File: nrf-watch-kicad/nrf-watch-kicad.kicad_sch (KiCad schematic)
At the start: 73 parts, among them IC1 TLV840MAPL36DBVRQ1, IC2 XC9265C181MR-G, IC3 TPS61023DRLT, IC4 MAX30101EFD+T, J1 Conn_ARM_JTAG_SWD_10, M1 Vibrator DC Motor, Q1 DMP2045U-7, Q2 S8050, U1 MAX1811ESA+, U2 DMC2400UV-7, U3 LIS2DS12TR, U4 MX25R6435FZNIL0, U5 u-blox ANNA-B402, U6 DRV2603RUNT, U7 XC9265A331MR-G, U8 TXB0104QRUTRQ1, U9 GC9A01

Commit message: Schematic pretty much done, final review left.
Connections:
- net ~{RESET_BAT_SUP}: now reaches IC1.1 (~{RESET}), IC2.3 (CE), TP7.1
- net TPS_VOUT: now reaches IC3.6 (VOUT), R17.2
- net BASE_BLK: now reaches Q2.2 (B), R14.2, R15.1
- net MOTOR_OUT-: now reaches M1.2 (-), U6.6 (OUT-)
- net MOTOR_OUT+: now reaches M1.1 (+), U6.9 (OUT+)
- net SELI: now reaches R2.1, U1.2 (SELI)
- net MR: now reaches IC1.4 (~{MR}), TP6.1
- net D_VOUT: now reaches L2.1, U7.4 (VOUT)
- net RESET_NN: now reaches J1.10 (~{RESET}), U5.12 (RESET_N/P0.18)
- net SWDIO: now reaches J1.2 (SWDIO/TMS), U5.42 (SWDIO)
- net SWDCLK: now reaches J1.4 (SWDCLK/TCK), U5.41 (SWDCLK)
- net COLLECTOR_BLK: now reaches Q2.3 (C), R16.1
- net DISPLAY_HIGH_DC: now reaches U8.10 (B1), U9.7 (D/C)
- net DISPLAY_HIGH_SDA: now reaches U8.7 (B4), U9.10 (SDA)
- net DISPLAY_HIGH_SCL: now reaches U8.8 (B3), U9.9 (SCL)
- net DISPLAY_HIGH_CS: now reaches U8.9 (B2), U9.8 (CS)
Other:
- note added: "1.8<->3.3 level shifter"
- note added: "5V regulator"
- note added: "Accelerometer and step counter"
- note added: "Biometric sensor Heart rate etc."
- note added: "Display"
- note added: "Display backlight"
- note added: "External 8MB Flash"
- note added: "Microcontroller (NRF52833)"
- note added: "Power Management"
- note added: "Power flags"
- note added: "Pull-up resistors"
- note added: "TODO CHECK if mosfet is correct connected"
- note added: "Vibration motor"
- note removed: "I2C pull-ups"
- note removed: "TODO CHECK if OK"
- company: (none) -> Jakob Krantz
- title: (none) -> Smart Watch
- moved on the sheet: BT1, C1, C10, C11, C12, C13, C14, C15, C16, C17, C18, C2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

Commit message: Started with routing.
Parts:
- removed NT1: NetTie_2, symbol Device:NetTie_2
- removed Q2: S8050, symbol Transistor_BJT:S8050
- removed TP4: GND, TestPoint:TestPoint_Pad_D2.0mm, symbol Connector:TestPoint
- added C19: 4.7uF, Capacitor_SMD:C_0603_1608Metric_Pad1.08x0.95mm_HandSolder, symbol Device:C_Small
- added CHG+1, EXT_VIN1: Conn_01x01_Male, TestPoint:TestPoint_Pad_D1.5mm, symbol Connector:Conn_01x01_Male
- added CHG-1, GND1: Conn_01x01_Male, TestPoint:TestPoint_Pad_1.5x1.5mm, symbol Connector:Conn_01x01_Male
- added Q2: SS8050-G, SamacSys_Parts:SOT95P240X115-3N, symbol SamacSys_Parts:SS8050-G
- BT1: footprint (none) -> Connector_Wire:SolderWire-0.1sqmm_1x02_P3.6mm_D0.4mm_OD1mm
- L1, L2, L3: footprint (none) -> Inductor_SMD:L_0603_1608Metric_Pad1.05x0.95mm_HandSolder
- M1: footprint (none) -> user_library:TestPoint_2Pads_Pitch2.54mm_Drill0.8mm
- TP5, TP8: footprint TestPoint:TestPoint_Pad_D2.0mm -> TestPoint:TestPoint_Pad_D1.0mm
- U5: footprint user_library:ANNA-B402 -> user_library:ANNA-B402_altium_import
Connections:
- net LEDA is gone; now on net DISPLAY_3V3: U9.3 (LEDA)
- net +1V8: now also C19.1
- net BASE_BLK: now also Q2.1
- net BAT_MON: now also U5.27 (GPIO_27/P0.31); no longer U5.24 (GPIO_24/P0.05)
- net BAT_MON_EN: now also U5.28 (GPIO_28/P0.30); no longer U5.29 (GPIO_29/P0.29)
- net COLLECTOR_BLK: now also Q2.3
- net DRV_VIB_PWM: now also U5.17 (GPIO_17/P0.00/XL1); no longer U5.33 (GPIO_33/P0.26)
- net GND: now also C19.2, CHG-1.1 (Pin_1), GND1.1 (Pin_1), Q2.2
- net INT1_LIS: now also U5.29 (GPIO_29/P0.29); no longer U5.50 (GPIO_50/P0.08)
- net INT2_LIS: now also U5.30 (GPIO_30/P0.28); no longer U5.11 (GPIO_11/P0.14)
- net VBUS: now also CHG+1.1 (Pin_1)
- net VDDA: now also EXT_VIN1.1 (Pin_1)
- net PWR_B4_BRIDGE: now reaches D1.1, IC1.2 (VDD), JP1.1 (A), Q1.3
- net D2: now reaches R6.1, U2.3 (D2)
- net G2: now reaches R4.2, U2.5 (G2), U2.6 (D1)
- net D_VOUT renamed V_VOUT
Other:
- moved on the sheet: C1

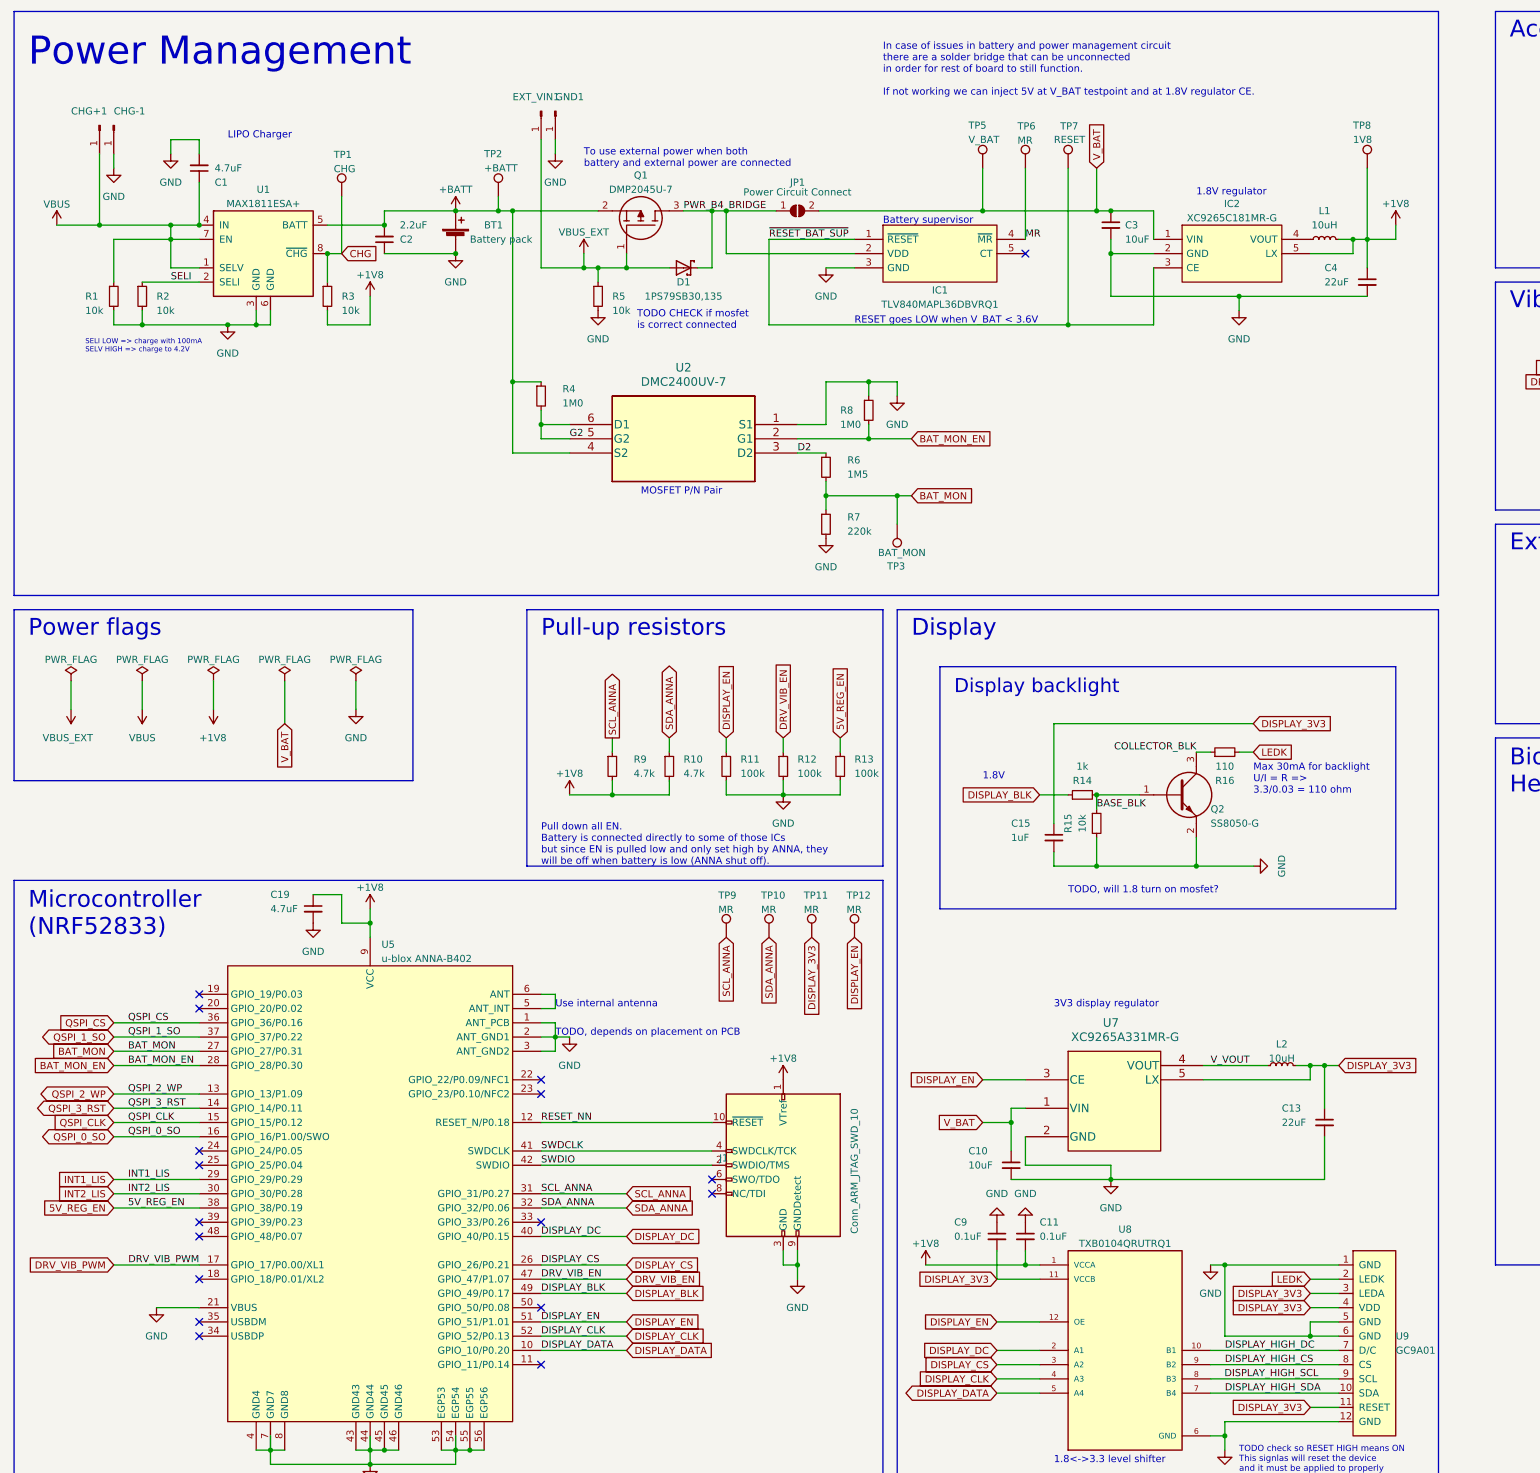
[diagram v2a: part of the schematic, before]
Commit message: Routed power, flash, accelerometer and vibration driver.
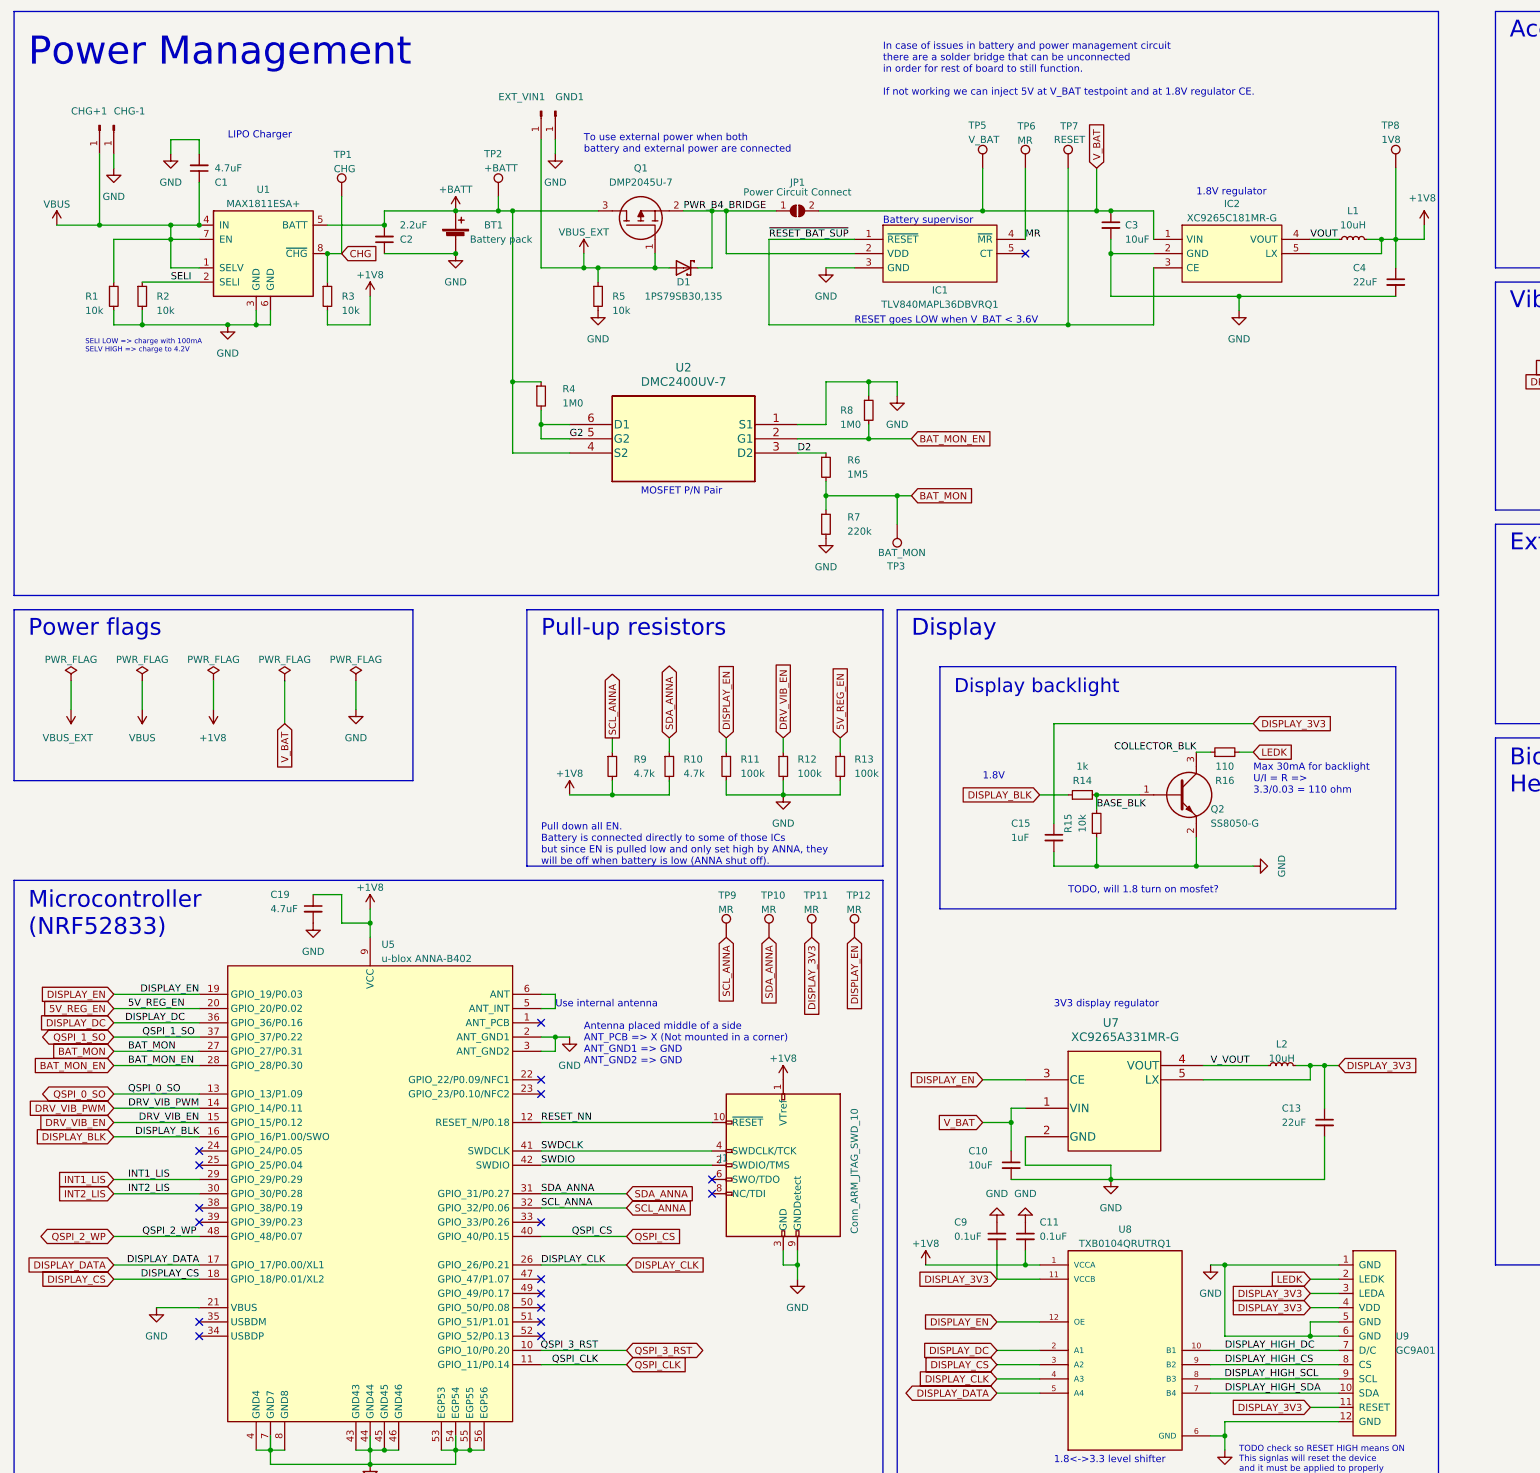
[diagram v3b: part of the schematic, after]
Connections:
- net +BATT: now also Q1.3; no longer Q1.2
- net 5V_REG_EN: now also U5.20 (GPIO_20/P0.02); no longer U5.38 (GPIO_38/P0.19)
- net DISPLAY_BLK: now also U5.16 (GPIO_16/P1.00/SWO); no longer U5.49 (GPIO_49/P0.17)
- net DISPLAY_CLK: now also U5.26 (GPIO_26/P0.21); no longer U5.52 (GPIO_52/P0.13)
- net DISPLAY_CS: now also U5.18 (GPIO_18/P0.01/XL2); no longer U5.26 (GPIO_26/P0.21)
- net DISPLAY_DATA: now also U5.17 (GPIO_17/P0.00/XL1); no longer U5.10 (GPIO_10/P0.20)
- net DISPLAY_DC: now also U5.36 (GPIO_36/P0.16); no longer U5.40 (GPIO_40/P0.15)
- net DISPLAY_EN: now also U5.19 (GPIO_19/P0.03); no longer U5.51 (GPIO_51/P1.01)
- net DRV_VIB_EN: now also U5.15 (GPIO_15/P0.12); no longer U5.47 (GPIO_47/P1.07)
- net DRV_VIB_PWM: now also U5.14 (GPIO_14/P0.11); no longer U5.17 (GPIO_17/P0.00/XL1)
- net GND: no longer U5.1 (ANT_PCB)
- net PWR_B4_BRIDGE: now also Q1.2; no longer Q1.3
- net QSPI_0_SO: now also U5.13 (GPIO_13/P1.09); no longer U5.16 (GPIO_16/P1.00/SWO)
- net QSPI_2_WP: now also U5.48 (GPIO_48/P0.07); no longer U5.13 (GPIO_13/P1.09)
- net QSPI_3_RST: now also U5.10 (GPIO_10/P0.20); no longer U5.14 (GPIO_14/P0.11)
- net QSPI_CLK: now also U5.11 (GPIO_11/P0.14); no longer U5.15 (GPIO_15/P0.12)
- net QSPI_CS: now also U5.40 (GPIO_40/P0.15); no longer U5.36 (GPIO_36/P0.16)
- net SCL_ANNA: now also U5.32 (GPIO_32/P0.06); no longer U5.31 (GPIO_31/P0.27)
- net SDA_ANNA: now also U5.31 (GPIO_31/P0.27); no longer U5.32 (GPIO_32/P0.06)
- net VOUT: now reaches IC2.4 (VOUT), L1.1
- no-connect marks 24 -> 25
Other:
- note added: "Antenna placed middle of a side ANT_PCB => X (Not mounted in a corner) ANT_GND1 => GND ANT_GND2 => GND"
- note removed: "TODO CHECK if mosfet is correct connected"
- note removed: "TODO, depends on placement on PCB"
- moved on the sheet: C4, L1, Q1, TP8

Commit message: All routed except test pads.
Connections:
- net TPS_VOUT is gone; now on net +5V: IC3.6 (VOUT), R17.2
- net +5V: no longer IC3.1 (FB), R17.1, R18.2
- net 5V_REG_EN: now also U5.27 (GPIO_27/P0.31); no longer U5.20 (GPIO_20/P0.02)
- net BAT_MON: now also U5.24 (GPIO_24/P0.05); no longer U5.27 (GPIO_27/P0.31)
- net BAT_MON_EN: now also U5.25 (GPIO_25/P0.04); no longer U5.28 (GPIO_28/P0.30)
- net DISPLAY_BLK: now also U5.33 (GPIO_33/P0.26); no longer U5.16 (GPIO_16/P1.00/SWO)
- net DISPLAY_CLK: now also U5.17 (GPIO_17/P0.00/XL1); no longer U5.26 (GPIO_26/P0.21)
- net DISPLAY_DATA: now also U5.16 (GPIO_16/P1.00/SWO); no longer U5.17 (GPIO_17/P0.00/XL1)
- net MAX30_INT: now also U5.28 (GPIO_28/P0.30)
- net SW: now reaches IC3.5 (SW), L3.2
- new net TPS_FB: IC3.1 (FB), R17.1, R18.2
- no-connect marks 25 -> 23
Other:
- moved on the sheet: C16

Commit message: Added and routed buttons.
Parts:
- removed GND1: Conn_01x01_Male, TestPoint:TestPoint_Pad_1.5x1.5mm, symbol Connector:Conn_01x01_Male
- removed J1: Conn_ARM_JTAG_SWD_10, Connector_PinHeader_1.27mm:PinHeader_2x05_P1.27mm_Vertical_SMD, symbol Connector:Conn_ARM_JTAG_SWD_10
- added S1, S2, S3: EVP-ATAL1B000, SamacSys_Parts:EVPATAL1B000, symbol SamacSys_Parts:EVP-ATAL1B000
- added TP4: MR, TestPoint:TestPoint_Pad_D1.0mm, symbol Connector:TestPoint
- TP2: value +BATT -> MR
- U4: 4MB variant (none) -> https://www.digikey.se/en/products/detail/macronix/MX25R323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
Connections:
- net +BATT: no longer TP2.1
- net DISPLAY_EN: no longer TP12.1
- net GND: now also S1.2 (COM), S2.2 (COM), S3.2 (COM); no longer U4.9 (EPAD)
- net SWDCLK: now also TP2.1
- net SWDIO: now also TP4.1
- net BTN_1: now reaches U5.20 (GPIO_20/P0.02)
- net BTN_1: now also S1.1 (NO)
- net BTN_2: now reaches U5.22 (GPIO_22/P0.09/NFC1)
- net BTN_2: now also S3.1 (NO)
- net BTN_3: now reaches U5.39 (GPIO_39/P0.23)
- net BTN_3: now also S2.1 (NO)
- net RESET_NN renamed RESET_N
- net RESET_N: now also TP12.1
- no-connect marks 23 -> 35

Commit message: Fix 1.8V and 3.3V regulator bug.
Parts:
- C16: value 2x22uF -> 47uF
- C6: value 100nF -> 10uF
- C7: value 10uF -> 100nF
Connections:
- net +1V8: now also IC2.4 (VOUT); no longer IC2.5 (LX)
- net BTN_2: now also S2.1 (NO), U5.39 (GPIO_39/P0.23); no longer S3.1 (NO), U5.22 (GPIO_22/P0.09/NFC1)
- net BTN_3: now also S3.1 (NO), U5.22 (GPIO_22/P0.09/NFC1); no longer S2.1 (NO), U5.39 (GPIO_39/P0.23)
- net DISPLAY_3V3: now also U7.4 (VOUT); no longer U7.5 (LX)
- net VOUT renamed LX_18
- net LX_18: now also IC2.5 (LX); no longer IC2.4 (VOUT)
- net V_VOUT renamed LX_3V3
- net LX_3V3: now also U7.5 (LX); no longer U7.4 (VOUT)
- no-connect marks 35 -> 29
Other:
- note added: "Buttons"
- note added: "Vibration motor (ERM Mode)"
- note removed: "Vibration motor"
